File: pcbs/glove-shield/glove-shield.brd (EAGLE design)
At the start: 54 x 51.8 mm, 19 parts, among them IC1 LM324D, IC2 LM324D, IC3 74LV4053PW

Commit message: Update bom and exported schematics
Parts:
- R27, R28, R4, R5, R6, R7, R8, R9: value (none) -> 15k
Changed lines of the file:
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@@
 <attribute name="VALUE" x="10.032" y="36.761" size="0.6096" layer="27" font="vector" ratio="20" rot="R90"/>
 </element>
-<element name="R4" library="SparkFun-Resistors" library_urn="urn:adsk.eagle:library:532" package="0603" package3d_urn="urn:adsk.eagle:package:39650/1" value=" " x="7" y="41" smashed="yes" rot="R90">
+<element name="R4" library="SparkFun-Resistors" library_urn="urn:adsk.eagle:library:532" package="0603" package3d_urn="urn:adsk.eagle:package:39650/1" value="15k" x="7" y="41" smashed="yes" rot="R90">
 <attribute name="NAME" x="6.238" y="41" size="0.6096" layer="25" font="vector" ratio="20" rot="R90" align="bottom-center"/>
 <attribute name="PROD_ID" value=" " x="7" y="41" size="1.778" layer="27" rot="R90" display="off"/>
 <attribute name="VALUE" x="7.762" y="41" size="0.6096" layer="27" font="vector" ratio="20" rot="R90" align="top-center"/>
 </element>
-<element name="R5" library="SparkFun-Resistors" library_urn="urn:adsk.eagle:library:532" package="0603" package3d_urn="urn:adsk.eagle:package:39650/1" value=" " x="7" y="34" smashed="yes" rot="R270">
+<element name="R5" library="SparkFun-Resistors" library_urn="urn:adsk.eagle:library:532" package="0603" package3d_urn="urn:adsk.eagle:package:39650/1" value="15k" x="7" y="34" smashed="yes" rot="R270">
 <attribute name="NAME" x="7.762" y="34" size="0.6096" layer="25" font="vector" ratio="20" rot="R270" align="bottom-center"/>
 <attribute name="PROD_ID" value=" " x="7" y="34" size="1.778" layer="27" rot="R270" display="off"/>
 <attribute name="VALUE" x="6.238" y="34" size="0.6096" layer="27" font="vector" ratio="20" rot="R270" align="top-center"/>
 </element>
-<element name="R6" library="SparkFun-Resistors" library_urn="urn:adsk.eagle:library:532" package="0603" package3d_urn="urn:adsk.eagle:package:39650/1" value=" " x="20" y="34" smashed="yes" rot="R270">
+<element name="R6" library="SparkFun-Resistors" library_urn="urn:adsk.eagle:library:532" package="0603" package3d_urn="urn:adsk.eagle:package:39650/1" value="15k" x="20" y="34" smashed="yes" rot="R270">
 <attribute name="NAME" x="20.762" y="34" size="0.6096" layer="25" font="vector" ratio="20" rot="R270" align="bottom-center"/>
 <attribute name="PROD_ID" value=" " x="20" y="34" size="1.778" layer="27" rot="R270" display="off"/>
 <attribute name="VALUE" x="19.238" y="34" size="0.6096" layer="27" font="vector" ratio="20" rot="R270" align="top-center"/>
 </element>
-<element name="R7" library="SparkFun-Resistors" library_urn="urn:adsk.eagle:library:532" package="0603" package3d_urn="urn:adsk.eagle:package:39650/1" value=" " x="20" y="41" smashed="yes" rot="R90">
+<element name="R7" library="SparkFun-Resistors" library_urn="urn:adsk.eagle:library:532" package="0603" package3d_urn="urn:adsk.eagle:package:39650/1" value="15k" x="20" y="41" smashed="yes" rot="R90">
 <attribute name="NAME" x="19.238" y="41" size="0.6096" layer="25" font="vector" ratio="20" rot="R90" align="bottom-center"/>
 <attribute name="PROD_ID" value=" " x="20" y="41" size="1.778" layer="27" rot="R90" display="off"/>
 <attribute name="VALUE" x="20.762" y="41" size="0.6096" layer="27" font="vector" ratio="20" rot="R90" align="top-center"/>
 </element>
-<element name="R8" library="SparkFun-Resistors" library_urn="urn:adsk.eagle:library:532" package="0603" package3d_urn="urn:adsk.eagle:package:39650/1" value=" " x="38.6698" y="40.5428" smashed="yes" rot="R90">
+<element name="R8" library="SparkFun-Resistors" library_urn="urn:adsk.eagle:library:532" package="0603" package3d_urn="urn:adsk.eagle:package:39650/1" value="15k" x="38.6698" y="40.5428" smashed="yes" rot="R90">
 <attribute name="NAME" x="35.9078" y="40.5428" size="0.6096" layer="25" font="vector" ratio="20" rot="R90" align="bottom-center"/>
 <attribute name="PROD_ID" value=" " x="38.6698" y="40.5428" size="1.778" layer="27" rot="R90" display="off"/>
 <attribute name="VALUE" x="39.4318" y="40.5428" size="0.6096" layer="27" font="vector" ratio="20" rot="R90" align="top-center"/>
 </element>
-<element name="R9" library="SparkFun-Resistors" library_urn="urn:adsk.eagle:library:532" package="0603" package3d_urn="urn:adsk.eagle:package:39650/1" value=" " x="39" y="34" smashed="yes" rot="R270">
+<element name="R9" library="SparkFun-Resistors" library_urn="urn:adsk.eagle:library:532" package="0603" package3d_urn="urn:adsk.eagle:package:39650/1" value="15k" x="39" y="34" smashed="yes" rot="R270">
 <attribute name="NAME" x="39.762" y="34" size="0.6096" layer="25" font="vector" ratio="20" rot="R270" align="bottom-center"/>
 <attribute name="PROD_ID" value=" " x="39" y="34" size="1.778" layer="27" rot="R270" display="off"/>
 <attribute name="VALUE" x="38.238" y="34" size="0.6096" layer="27" font="vector" ratio="20" rot="R270" align="top-center"/>
 </element>
-<element name="R27" library="SparkFun-Resistors" library_urn="urn:adsk.eagle:library:532" package="0603" package3d_urn="urn:adsk.eagle:package:39650/1" value=" " x="26" y="34" smashed="yes" rot="R270">
+<element name="R27" library="SparkFun-Resistors" library_urn="urn:adsk.eagle:library:532" package="0603" package3d_urn="urn:adsk.eagle:package:39650/1" value="15k" x="26" y="34" smashed="yes" rot="R270">
 <attribute name="NAME" x="26.762" y="34" size="0.6096" layer="25" font="vector" ratio="20" rot="R270" align="bottom-center"/>
 <attribute name="PROD_ID" value=" " x="26" y="34" size="1.778" layer="27" rot="R270" display="off"/>
 <attribute name="VALUE" x="25.238" y="34" size="0.6096" layer="27" font="vector" ratio="20" rot="R270" align="top-center"/>
 </element>
-<element name="R28" library="SparkFun-Resistors" library_urn="urn:adsk.eagle:library:532" package="0603" package3d_urn="urn:adsk.eagle:package:39650/1" value=" " x="26" y="41" smashed="yes" rot="R90">
+<element name="R28" library="SparkFun-Resistors" library_urn="urn:adsk.eagle:library:532" package="0603" package3d_urn="urn:adsk.eagle:package:39650/1" value="15k" x="26" y="41" smashed="yes" rot="R90">
 <attribute name="NAME" x="25.238" y="41" size="0.6096" layer="25" font="vector" ratio="20" rot="R90" align="bottom-center"/>
 <attribute name="PROD_ID" value=" " x="26" y="41" size="1.778" layer="27" rot="R90" display="off"/>

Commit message: Updated glove shield pcb design
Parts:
- removed IC3: 74LV4053PW, toy-mech:SOT403-1_NEX
- added IC4: 4052D, 40xx:SO16
- moved C2 2.00 mm to (47.0, 44.0)
- moved R9 1.00 mm to (38.0, 34.0)
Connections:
- removed net N$29: B1.A2, IC3.4
- new net N$1: B1.D13, IC4.9
- net 5V: now also IC4.16; no longer IC3.16
- net ADC1: now also IC4.2; no longer IC3.1
- net ADC2: now also IC4.14; no longer IC3.2
- net ADC3: now also IC4.12; no longer IC3.3
- net ADC4: now also IC4.5; no longer IC3.5
- net ADC5: now also IC4.1; no longer IC3.13
- net ADC6: now also IC4.11; no longer IC3.12
- net ADC7: now also IC4.4; no longer B1.A4
- net ADC8: now also IC4.15; no longer B1.A3
- net COM: now also IC4.6, IC4.7, IC4.8; no longer IC3.6, IC3.7, IC3.8
- net N$26: now also IC4.3; no longer IC3.15
- net N$31: now also IC4.10; no longer IC3.10, IC3.11, IC3.9
- net N$9: now also IC4.13; no longer IC3.14
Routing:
- net N$1: track 0.00 -> 56.3 mm, vias 0 -> 1
- net 5V: track 156.1 -> 173.3 mm
- net N$29: track 17.0 -> 0.00 mm
- net ADC7: track 33.8 -> 22.1 mm, vias 1 -> 2
- net ADC5: track 32.0 -> 21.7 mm
- net N$26: track 7.10 -> 15.3 mm
- net ADC6: track 24.4 -> 20.3 mm
- net ADC8: track 21.6 -> 17.6 mm, vias 1 -> 2
- net ADC2: track 37.4 -> 39.8 mm
- net FLEX7IN: track 18.6 -> 20.5 mm
- net ADC1: track 34.5 -> 35.7 mm
- net ADC3: track 39.4 -> 38.2 mm
- net N$9: track 5.21 -> 6.11 mm
- net ADC4: track 32.5 -> 31.7 mm
- net N$31: track 54.9 -> 54.3 mm
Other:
- board text added: "Mini Mech Glove Shield Rev 3. 10/06/2021"
- board text removed: "Mini Mech Glove Shield Rev 2. 08/17/2021"

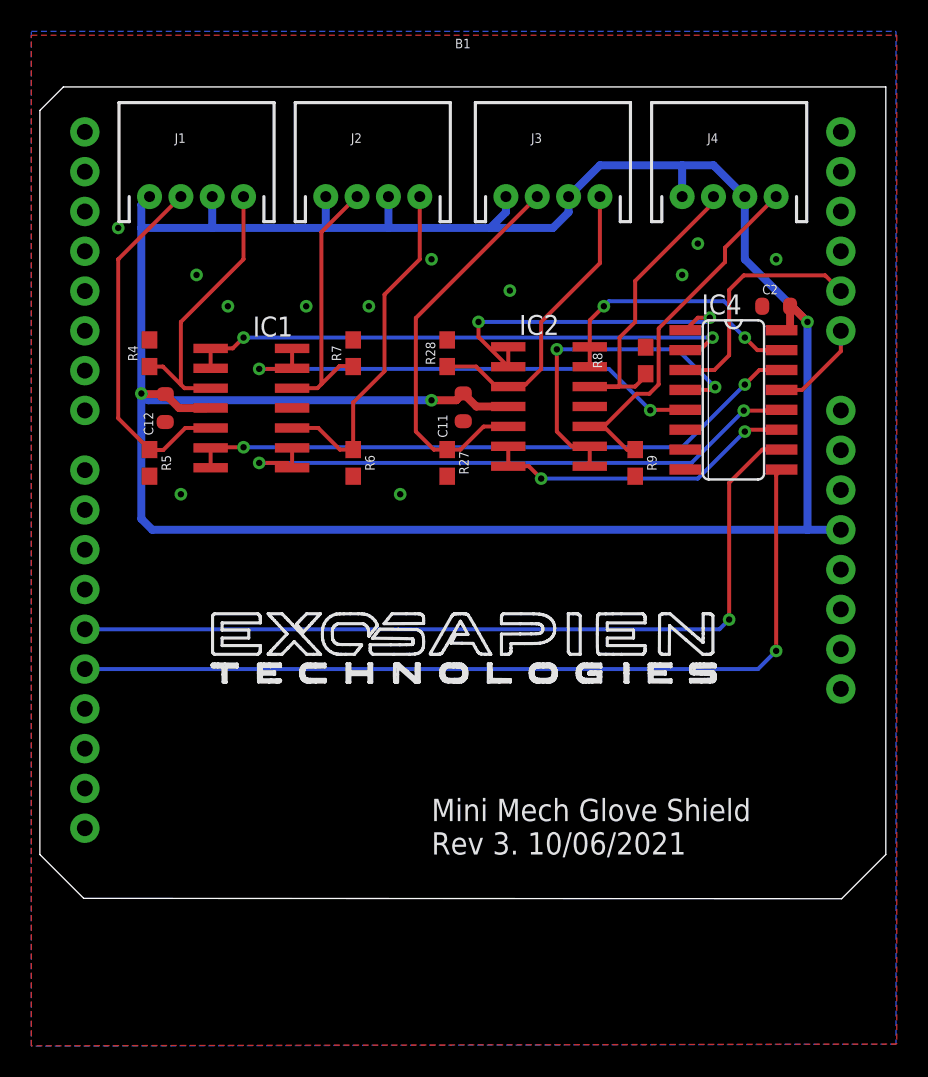
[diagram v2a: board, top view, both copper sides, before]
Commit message: Updated boards to latest, updated bom export, and CAM exports
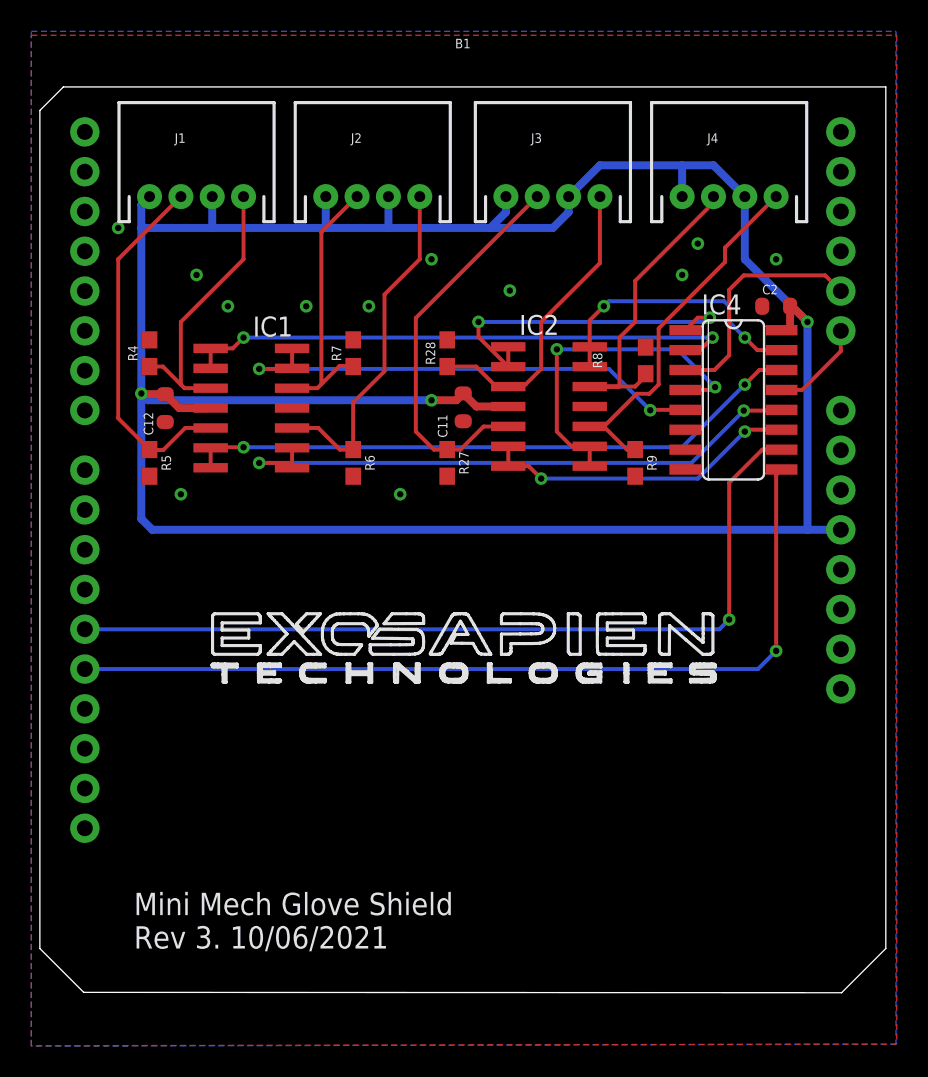
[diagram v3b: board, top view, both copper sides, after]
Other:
- board size 54 x 51.8 mm -> 54 x 57.8 mm
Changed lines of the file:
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@@
 <board>
 <plain>
-<wire x1="0" y1="56.5" x2="0" y2="9" width="0" layer="20"/>
-<wire x1="54" y1="9" x2="54" y2="58" width="0" layer="20"/>
+<wire x1="0" y1="56.5" x2="0" y2="3" width="0" layer="20"/>
+<wire x1="54" y1="3" x2="54" y2="58" width="0" layer="20"/>
 <circle x="23.454" y="33.8194" radius="0.1436" width="0.4064" layer="22"/>
 <circle x="1.778" y="14.351" radius="0.340775" width="0.4064" layer="140"/>
@@
 <wire x1="0" y1="56.5" x2="1.5" y2="58" width="0" layer="20"/>
 <wire x1="1.5" y1="58" x2="54" y2="58" width="0" layer="20"/>
-<wire x1="51.1778" y1="6.1778" x2="54" y2="9" width="0" layer="20"/>
-<text x="25" y="9" size="1.4224" layer="25" font="vector">Mini Mech Glove Shield
+<wire x1="51.1778" y1="0.1778" x2="54" y2="3" width="0" layer="20"/>
+<text x="6" y="3" size="1.4224" layer="25" font="vector">Mini Mech Glove Shield
 Rev 3. 10/06/2021</text>
-<wire x1="51.1778" y1="6.1778" x2="2.7968" y2="6.2032" width="0" layer="20"/>
-<wire x1="2.7968" y1="6.2032" x2="0" y2="9" width="0" layer="20"/>
+<wire x1="51.1778" y1="0.1778" x2="2.7968" y2="0.2032" width="0" layer="20"/>
+<wire x1="2.7968" y1="0.2032" x2="0" y2="3" width="0" layer="20"/>
 <wire x1="13.9874" y1="21.84236875" x2="14.027703125" y2="21.884978125" width="0.2" layer="25" curve="11.785537"/>
 <wire x1="14.0277" y1="21.88498125" x2="14.049171875" y2="21.927553125" width="0.2" layer="25" curve="21.493738"/>
